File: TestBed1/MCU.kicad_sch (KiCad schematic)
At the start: 0 parts

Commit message: WIP Adding new sheets.
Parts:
- added C4: C, symbol Device:C
- added J5: TAG_CONNECT, Connector:Tag-Connect_TC2030-IDC-FP_2x03_P1.27mm_Vertical, symbol ACTempDisconnect:TAG_CONNECT
- added U1: STM32G0B1KBTx, Package_QFP:LQFP-32_7x7mm_P0.8mm, symbol MCU_ST_STM32G0:STM32G0B1KBTx
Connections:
- new net +3V3: C4.1, U1.4 (VDD)
- new net GND: C4.2, J5.3 (GND), U1.5 (VSS)
- new net SWDCLK: J5.5 (SWCLK)
- new net SWDIO: J5.6 (SWDIO)
- new net VCC: J5.1 (POWER_3V3)
- no-connect marks 0 -> 2
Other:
- note removed: "TODO CAN Transceiver"
- note removed: "TODO MCU"

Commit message: WIP - Parts Assigned
Need footprints, and MCU connections, but WIP
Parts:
- added J6: Conn_01x02_Pin, Connector_PinHeader_1.27mm:PinHeader_1x02_P1.27mm_Vertical, symbol Connector:Conn_01x02_Pin
- added R6: TBD, symbol Device:R
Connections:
- net GND: now also J6.1 (Pin_1), R6.2
- new net AMB_OUT: J6.2 (Pin_2), R6.1
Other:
- note added: "1uA->50uA based on no light to all light"
- note added: "Connector for decade box for testing"

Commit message: Rough Grouping, Passive Footprint Assignment
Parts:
- C4: value C -> 0.1u; footprint (none) -> Capacitor_SMD:C_0402_1005Metric_Pad0.74x0.62mm_HandSolder
- R6: footprint (none) -> Resistor_SMD:R_0402_1005Metric
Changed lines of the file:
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@@
 			)
 		)
-		(property "Value" "C"
+		(property "Value" "0.1u"
 			(at 90.17 45.7199 0)
 			(effects
@@
 			)
 		)
-		(property "Footprint" ""
+		(property "Footprint" "Capacitor_SMD:C_0402_1005Metric_Pad0.74x0.62mm_HandSolder"
 			(at 87.3252 48.26 0)
 			(effects
@@
 			)
 		)
-		(property "Footprint" ""
+		(property "Footprint" "Resistor_SMD:R_0402_1005Metric"
 			(at 215.392 127 90)
 			(effects

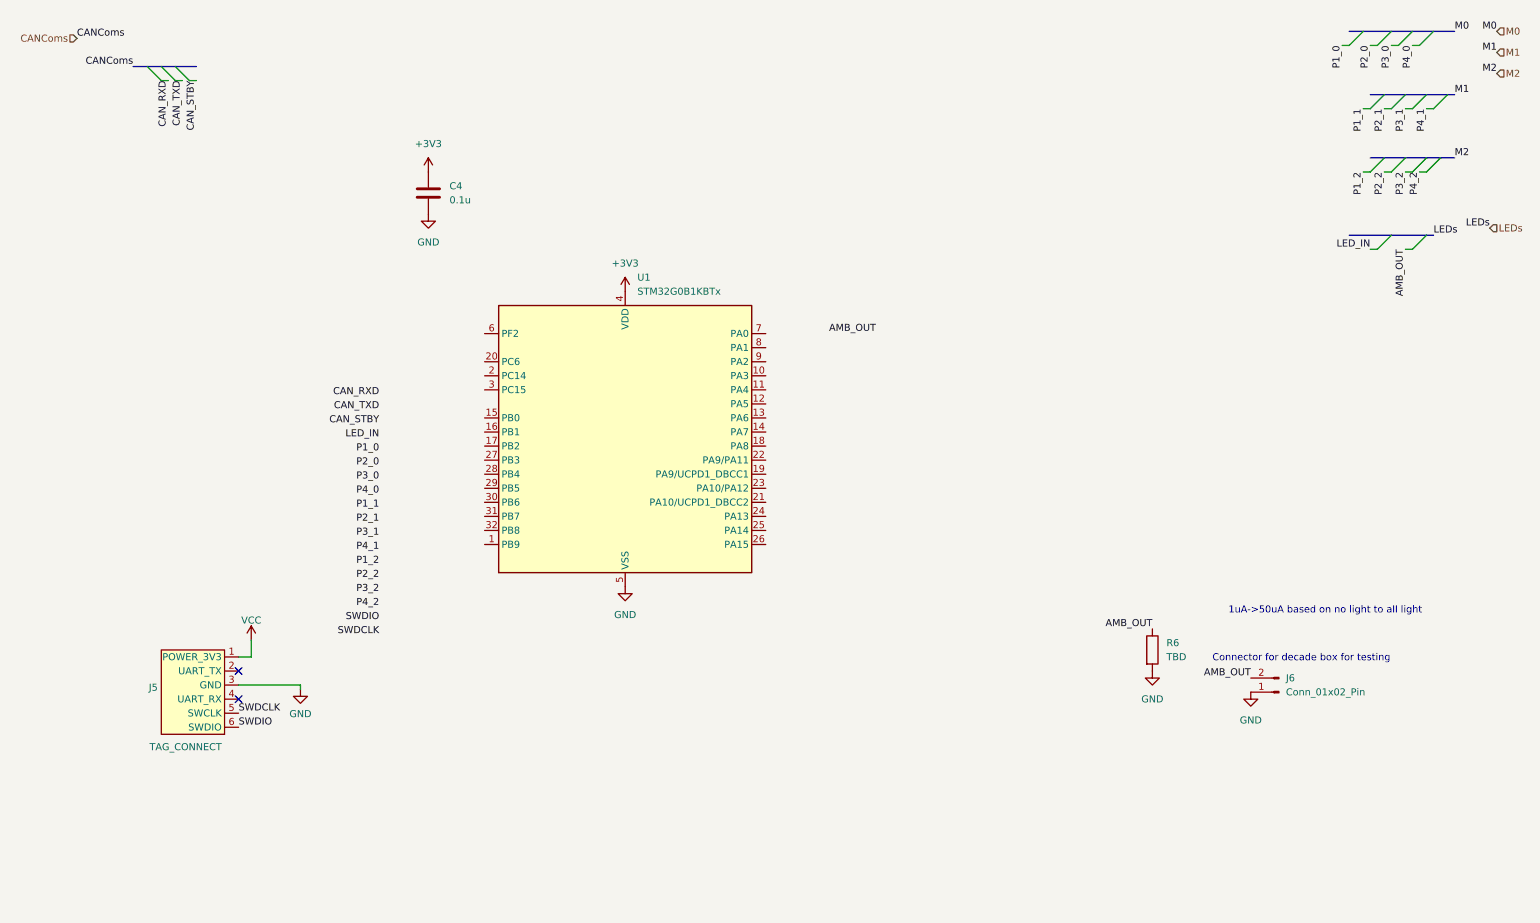
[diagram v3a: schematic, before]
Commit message: Schematic Assignment, board assignemtn and rough placement
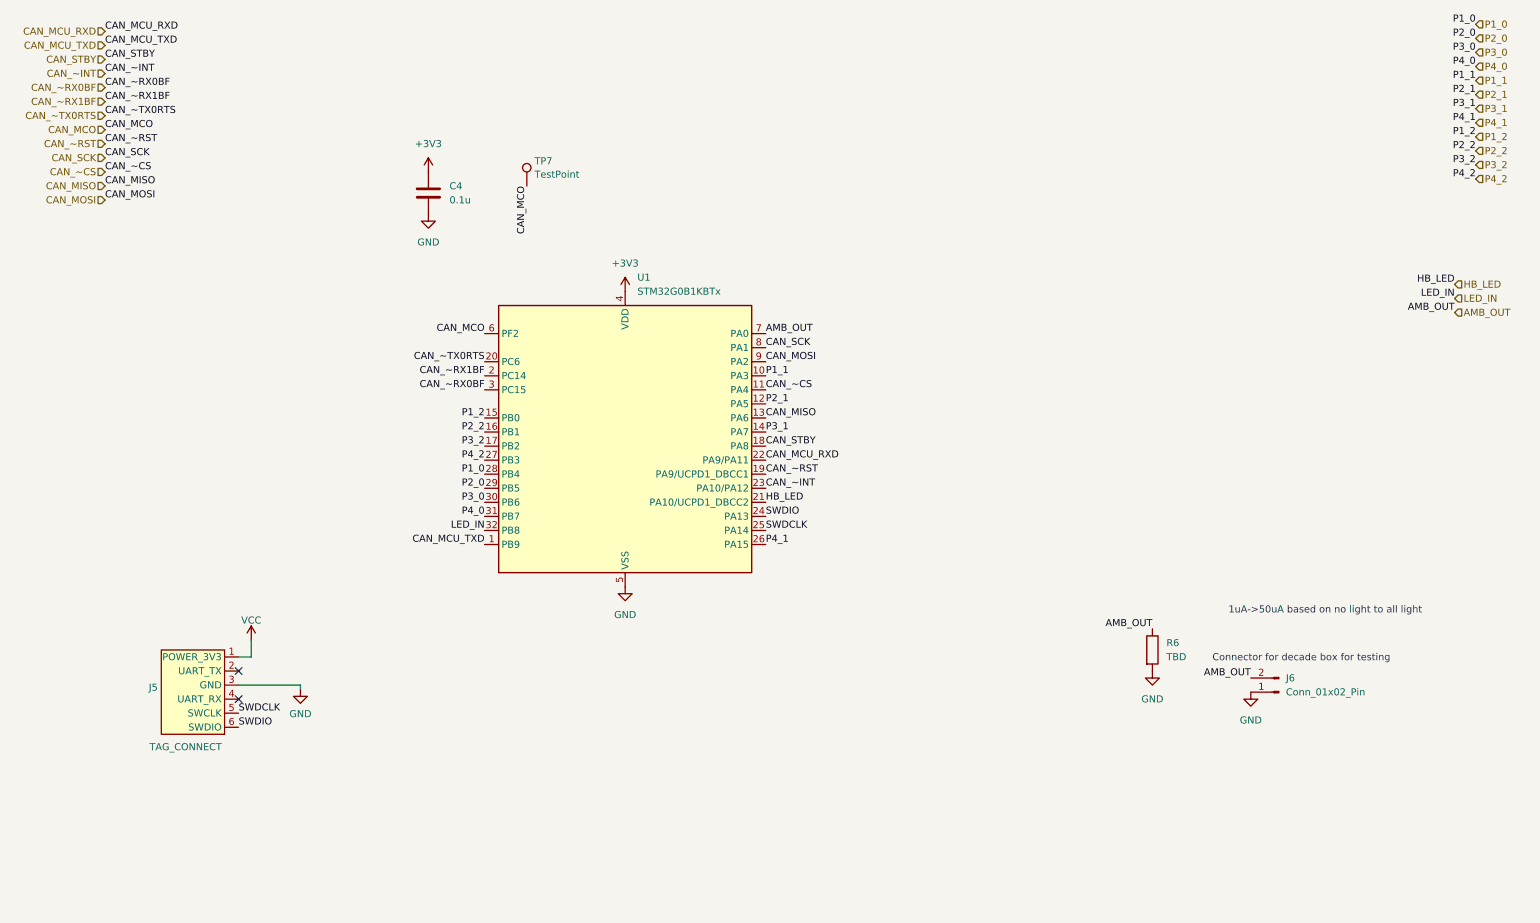
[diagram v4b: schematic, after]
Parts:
- added TP7: TestPoint, TestPoint:TestPoint_Pad_1.0x1.0mm, symbol Connector:TestPoint
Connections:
- net AMB_OUT: now also U1.7 (PA0)
- net CAN_STBY: now also U1.18 (PA8)
- net LED_IN: now also U1.32 (PB8)
- net P1_0: now also U1.28 (PB4)
- net P1_1: now also U1.10 (PA3)
- net P1_2: now also U1.15 (PB0)
- net P2_0: now also U1.29 (PB5)
- net P2_1: now also U1.12 (PA5)
- net P2_2: now also U1.16 (PB1)
- net P3_0: now also U1.30 (PB6)
- net P3_1: now also U1.14 (PA7)
- net P3_2: now also U1.17 (PB2)
- net P4_0: now also U1.31 (PB7)
- net P4_1: now also U1.26 (PA15)
- net P4_2: now also U1.27 (PB3)
- net SWDCLK: now also U1.25 (PA14)
- net SWDIO: now also U1.24 (PA13)
- net CAN_MCU_TXD: now reaches U1.1 (PB9)
- net CAN_~CS: now reaches U1.11 (PA4)
- net CAN_MISO: now reaches U1.13 (PA6)
- net CAN_~RST: now reaches U1.19 (PA9/UCPD1_DBCC1)
- net CAN_~RX1BF: now reaches U1.2 (PC14)
- net CAN_~TX0RTS: now reaches U1.20 (PC6)
- net HB_LED: now reaches U1.21 (PA10/UCPD1_DBCC2)
- net CAN_MCU_RXD: now reaches U1.22 (PA9/PA11)
- net CAN_~INT: now reaches U1.23 (PA10/PA12)
- net CAN_~RX0BF: now reaches U1.3 (PC15)
- net CAN_MCO: now reaches U1.6 (PF2)
- net CAN_MCO: now also TP7.1
- net CAN_SCK: now reaches U1.8 (PA1)
- net CAN_MOSI: now reaches U1.9 (PA2)

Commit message: WIP - routing
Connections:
- net VCC is gone; now on net +3V3: J5.1 (POWER_3V3)
- net CAN_STBY: no longer U1.18 (PA8)
- net CAN_~CS: no longer U1.11 (PA4)
- net CAN_~INT: now also U1.30 (PB6); no longer U1.23 (PA10/PA12)
- net CAN_~RST: now also U1.31 (PB7); no longer U1.19 (PA9/UCPD1_DBCC1)
- net CAN_~RX0BF: now also U1.15 (PB0); no longer U1.3 (PC15)
- net CAN_~RX1BF: now also U1.16 (PB1); no longer U1.2 (PC14)
- net CAN_~TX0RTS: now also U1.32 (PB8); no longer U1.20 (PC6)
- net HB_LED: now also U1.20 (PC6); no longer U1.21 (PA10/UCPD1_DBCC2)
- net LED_IN: now also U1.17 (PB2); no longer U1.32 (PB8)
- net P1_1: no longer U1.10 (PA3)
- net P1_2: now also U1.21 (PA10/UCPD1_DBCC2); no longer U1.15 (PB0)
- net P2_1: no longer U1.12 (PA5)
- net P2_2: now also U1.23 (PA10/PA12); no longer U1.16 (PB1)
- net P3_0: now also U1.26 (PA15); no longer U1.30 (PB6)
- net P3_2: now also U1.18 (PA8); no longer U1.17 (PB2)
- net P4_0: now also U1.27 (PB3); no longer U1.31 (PB7)
- net P4_1: now also U1.3 (PC15); no longer U1.26 (PA15)
- net P4_2: now also U1.19 (PA9/UCPD1_DBCC1); no longer U1.27 (PB3)
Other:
- moved on the sheet: J5
